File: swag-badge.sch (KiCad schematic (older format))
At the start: 22 parts, among them J1 OLED_1, J10 Edge_pad, J11 Edge_pad, J12 Breakout_LHS, J13 Breakout_RHS, J2 OLED_2, J3 SAO_1, J4 SAO_2, J5 SAO_3, J6 SAO_4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

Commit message: Minor footprint work
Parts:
- added H3: MountingHole, SwagBadge:Lanyard_Hole_3mm, symbol Mechanical:MountingHole
- J12: renamed from J13; value Breakout_RHS -> Breakout_LHS; footprint Pin_Headers:Pin_Header_Angled_1x08_Pitch2.54mm -> SwagBadge:Pin_Header_Angled_1x08_Pitch2.54mm
- J13: renamed from J12; value Breakout_LHS -> Breakout_RHS; footprint Pin_Headers:Pin_Header_Angled_1x08_Pitch2.54mm -> SwagBadge:Pin_Header_Angled_1x08_Pitch2.54mm
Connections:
- net +3V3: now also J12.8 (Pin_8), J13.8 (Pin_8); no longer J12.1 (Pin_1), J13.1 (Pin_1)
- net GND: now also J12.1 (Pin_1), J13.1 (Pin_1); no longer J12.8 (Pin_8), J13.8 (Pin_8)
- net GPIO0: now also J12.4 (Pin_4); no longer J12.5 (Pin_5)
- net GPIO13: now also J12.2 (Pin_2); no longer J12.7 (Pin_7)
- net GPIO18: now also J12.7 (Pin_7); no longer J12.2 (Pin_2)
- net GPIO2: now also J12.3 (Pin_3); no longer J12.6 (Pin_6)
- net GPIO25: now also J13.3 (Pin_3); no longer J13.6 (Pin_6)
- net GPIO26: now also J13.2 (Pin_2); no longer J13.7 (Pin_7)
- net GPIO32: now also J13.5 (Pin_5); no longer J13.4 (Pin_4)
- net GPIO33: now also J13.4 (Pin_4); no longer J13.5 (Pin_5)
- net GPIO34: now also J13.7 (Pin_7); no longer J13.2 (Pin_2)
- net GPIO35: now also J13.6 (Pin_6); no longer J13.3 (Pin_3)
- net GPIO4: now also J12.5 (Pin_5); no longer J12.4 (Pin_4)
- net GPIO5: now also J12.6 (Pin_6); no longer J12.3 (Pin_3)
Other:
- moved on the sheet: J13
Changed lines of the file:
@@
-$EndComp
-$Comp
-L Connector_Generic:Conn_01x08 J13
-U 1 1 5F7E62CC
-P 7800 2000
-F 0 "J13" H 7750 2500 50  0000 L CNN
-F 1 "Breakout_RHS" H 7700 2400 50  0000 L CNN
-F 2 "Pin_Headers:Pin_Header_Angled_1x08_Pitch2.54mm" H 7800 2000 50  0001 C CNN
-F 3 "~" H 7800 2000 50  0001 C CNN
-	1    7800 2000
-	-1   0    0    -1
 $EndComp
 $Comp
@@
 $EndComp
 $Comp
-L power:+3V3 #PWR?
+L power:+3V3 #PWR0115
 U 1 1 5F810C4A
 P 8150 1600
-F 0 "#PWR?" H 8150 1450 50  0001 C CNN
+F 0 "#PWR0115" H 8150 1450 50  0001 C CNN
 F 1 "+3V3" H 8165 1773 50  0000 C CNN
 F 2 "" H 8150 1600 50  0001 C CNN
@@
 $EndComp
 $Comp
-L power:GND #PWR?
+L power:GND #PWR0116
 U 1 1 5F816772
-P 6350 2500
-F 0 "#PWR?" H 6350 2250 50  0001 C CNN
-F 1 "GND" H 6355 2327 50  0000 C CNN
-F 2 "" H 6350 2500 50  0001 C CNN
-F 3 "" H 6350 2500 50  0001 C CNN
-	1    6350 2500
+P 8850 2500
+F 0 "#PWR0116" H 8850 2250 50  0001 C CNN
+F 1 "GND" H 8855 2327 50  0000 C CNN
+F 2 "" H 8850 2500 50  0001 C CNN
+F 3 "" H 8850 2500 50  0001 C CNN
+	1    8850 2500
 	1    0    0    -1
 $EndComp
 $Comp
-L power:GND #PWR?
+L power:GND #PWR0117
 U 1 1 5F816BF9
 P 8100 2500
-F 0 "#PWR?" H 8100 2250 50  0001 C CNN
+F 0 "#PWR0117" H 8100 2250 50  0001 C CNN
 F 1 "GND" H 8105 2327 50  0000 C CNN
 F 2 "" H 8100 2500 50  0001 C CNN
@@
 $EndComp
 Wire Wire Line
-	6450 2400 6350 2400
+	8950 2400 8850 2400
 Wire Wire Line
-	6350 2400 6350 2500
+	8850 2400 8850 2500
 Wire Wire Line
 	8000 2400 8100 2400
@@
 	8150 1700 8150 1600
 Wire Wire Line
-	6450 1700 6350 1700
+	8950 1700 8850 1700
 Wire Wire Line
-	6350 1700 6350 1600
+	8850 1700 8850 1600
 Text Label 8400 2200 2    70   ~ 0
 GPIO2
@@
 Wire Wire Line
 	8000 2300 8400 2300
-Text Label 6050 1800 0    70   ~ 0
+Text Label 8550 1800 0    70   ~ 0
 GPIO34
-Text Label 6050 1900 0    70   ~ 0
+Text Label 8550 1900 0    70   ~ 0
 GPIO35
-Text Label 6050 2000 0    70   Italic 0
+Text Label 8550 2000 0    70   Italic 0
 GPIO32
-Text Label 6050 2100 0    70   Italic 0
+Text Label 8550 2100 0    70   Italic 0
 GPIO33
-Text Label 6050 2200 0    70   Italic 0
+Text Label 8550 2200 0    70   Italic 0
 GPIO25
-Text Label 6050 2300 0    70   Italic 0
+Text Label 8550 2300 0    70   Italic 0
 GPIO26
 Wire Wire Line
-	6450 2300 6050 2300
+	8950 2300 8550 2300
 Wire Wire Line
-	6050 2200 6450 2200
+	8550 2200 8950 2200
 Wire Wire Line
-	6050 2100 6450 2100
+	8550 2100 8950 2100
 Wire Wire Line
-	6050 2000 6450 2000
+	8550 2000 8950 2000
 Wire Wire Line
-	6050 1900 6450 1900
+	8550 1900 8950 1900
 Wire Wire Line
-	6050 1800 6450 1800
+	8550 1800 8950 1800
 $Comp
 L Mechanical:MountingHole H4
@@
 $EndComp
 $Comp
-L Connector_Generic:Conn_01x08 J12
-U 1 1 5F7FE834
-P 6650 2000
-F 0 "J12" H 6600 2550 50  0000 L CNN
-F 1 "Breakout_LHS" H 6400 2450 50  0000 L CNN
-F 2 "Pin_Headers:Pin_Header_Angled_1x08_Pitch2.54mm" H 6650 2000 50  0001 C CNN
-F 3 "~" H 6650 2000 50  0001 C CNN
-	1    6650 2000
-	1    0    0    -1
-$EndComp
-$Comp
-L power:+3V3 #PWR?
+L power:+3V3 #PWR0118
 U 1 1 5F85A5CE
-P 6350 1600
-F 0 "#PWR?" H 6350 1450 50  0001 C CNN
-F 1 "+3V3" H 6365 1773 50  0000 C CNN
-F 2 "" H 6350 1600 50  0001 C CNN
-F 3 "" H 6350 1600 50  0001 C CNN
-	1    6350 1600
+P 8850 1600
+F 0 "#PWR0118" H 8850 1450 50  0001 C CNN
+F 1 "+3V3" H 8865 1773 50  0000 C CNN
+F 2 "" H 8850 1600 50  0001 C CNN
+F 3 "" H 8850 1600 50  0001 C CNN
+	1    8850 1600
 	1    0    0    -1
 $EndComp
 Text Label 8400 2300 2    70   ~ 0
 GPIO13
+$Comp
+L Connector_Generic:Conn_01x08 J13
+U 1 1 5F7FE834
+P 9150 2100
+F 0 "J13" H 9050 1450 50  0000 L CNN
+F 1 "Breakout_RHS" H 8900 1550 50  0000 L CNN
+F 2 "SwagBadge:Pin_Header_Angled_1x08_Pitch2.54mm" H 9150 2100 50  0001 C CNN
+F 3 "~" H 9150 2100 50  0001 C CNN
+	1    9150 2100
+	1    0    0    1
+$EndComp
+$Comp
+L Connector_Generic:Conn_01x08 J12
+U 1 1 5F7E62CC
+P 7800 2100
+F 0 "J12" H 7750 1450 50  0000 L CNN
+F 1 "Breakout_LHS" H 7600 1550 50  0000 L CNN
+F 2 "SwagBadge:Pin_Header_Angled_1x08_Pitch2.54mm" H 7800 2100 50  0001 C CNN
+F 3 "~" H 7800 2100 50  0001 C CNN
+	1    7800 2100
+	-1   0    0    1
+$EndComp
+$Comp
+L Mechanical:MountingHole H3
+U 1 1 5F800940
+P 5800 6400
+F 0 "H3" H 5900 6446 50  0000 L CNN
+F 1 "MountingHole" H 5900 6355 50  0000 L CNN
+F 2 "SwagBadge:Lanyard_Hole_3mm" H 5800 6400 50  0001 C CNN
+F 3 "~" H 5800 6400 50  0001 C CNN
+	1    5800 6400
+	1    0    0    -1
+$EndComp
 $EndSCHEMATC

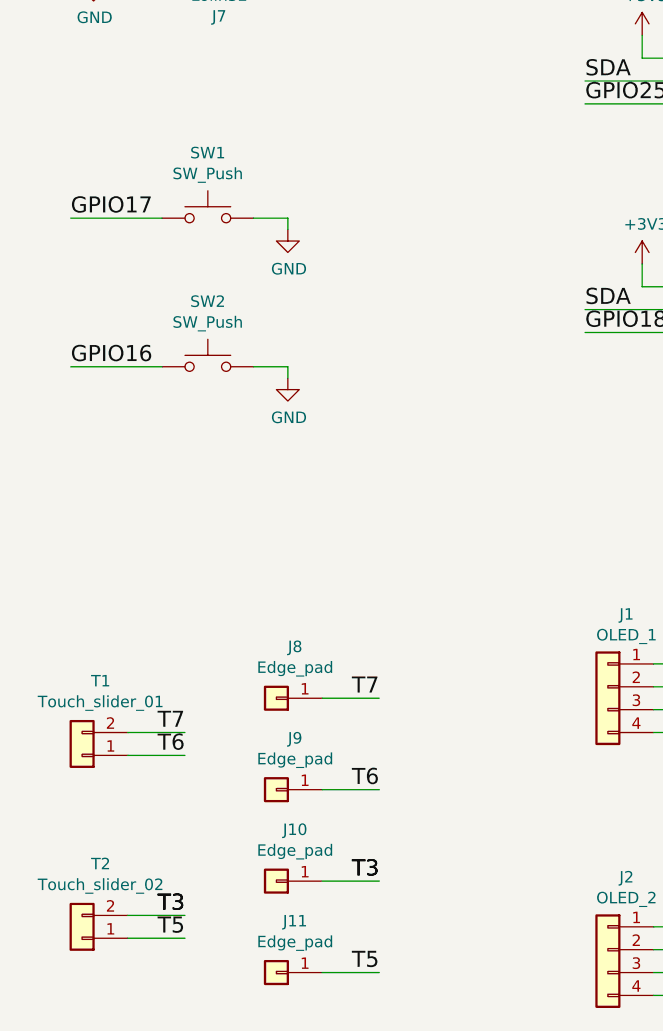
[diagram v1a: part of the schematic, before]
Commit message: Updated Component names to reflect purpose.
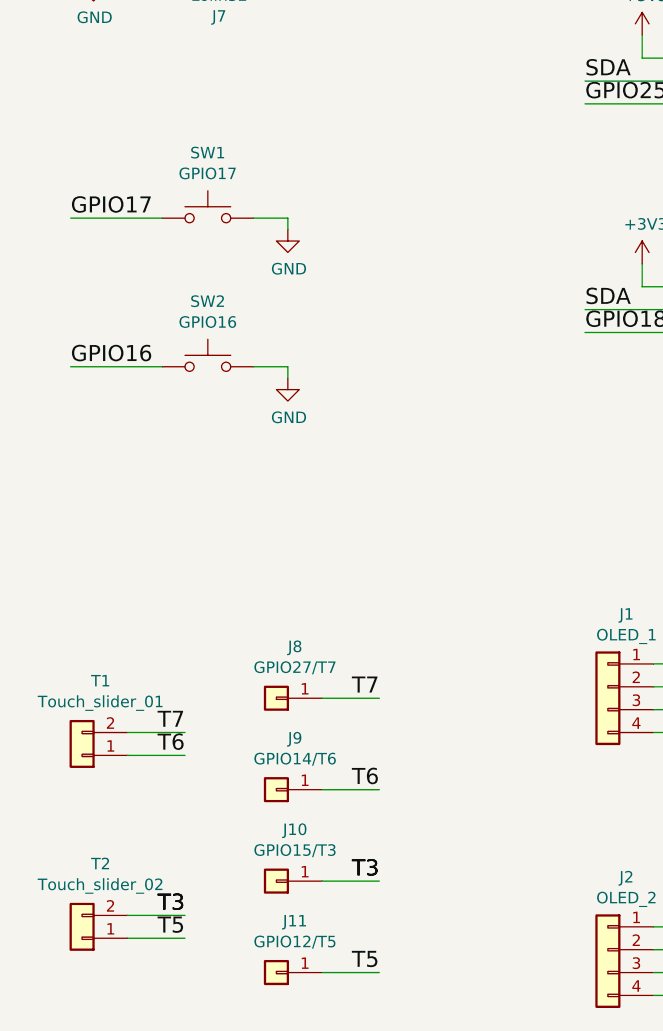
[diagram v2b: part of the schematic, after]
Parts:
- J10: value Edge_pad -> GPIO15/T3
- J11: value Edge_pad -> GPIO12/T5
- J8: value Edge_pad -> GPIO27/T7
- J9: value Edge_pad -> GPIO14/T6
- SW1: value SW_Push -> GPIO17
- SW2: value SW_Push -> GPIO16
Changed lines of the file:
@@
 P 1800 3700
 F 0 "SW1" H 1800 3985 50  0000 C CNN
-F 1 "SW_Push" H 1800 3894 50  0000 C CNN
+F 1 "GPIO17" H 1800 3894 50  0000 C CNN
 F 2 "SwagBadge:SW_SPST_6x3mm" H 1800 3900 50  0001 C CNN
 F 3 "~" H 1800 3900 50  0001 C CNN
@@
 P 1800 4350
 F 0 "SW2" H 1800 4635 50  0000 C CNN
-F 1 "SW_Push" H 1800 4544 50  0000 C CNN
+F 1 "GPIO16" H 1800 4544 50  0000 C CNN
 F 2 "SwagBadge:SW_SPST_6x3mm" H 1800 4550 50  0001 C CNN
 F 3 "~" H 1800 4550 50  0001 C CNN
@@
 P 2100 5800
 F 0 "J8" H 2018 5575 50  0000 C CNN
-F 1 "Edge_pad" H 2018 5666 50  0000 C CNN
+F 1 "GPIO27/T7" H 2018 5666 50  0000 C CNN
 F 2 "SwagBadge:Strain_Pad" H 2100 5800 50  0001 C CNN
 F 3 "~" H 2100 5800 50  0001 C CNN
@@
 P 2100 6200
 F 0 "J9" H 2018 5975 50  0000 C CNN
-F 1 "Edge_pad" H 2018 6066 50  0000 C CNN
+F 1 "GPIO14/T6" H 2018 6066 50  0000 C CNN
 F 2 "SwagBadge:Strain_Pad" H 2100 6200 50  0001 C CNN
 F 3 "~" H 2100 6200 50  0001 C CNN
@@
 P 2100 6600
 F 0 "J10" H 2018 6375 50  0000 C CNN
-F 1 "Edge_pad" H 2018 6466 50  0000 C CNN
+F 1 "GPIO15/T3" H 2018 6466 50  0000 C CNN
 F 2 "SwagBadge:Strain_Pad" H 2100 6600 50  0001 C CNN
 F 3 "~" H 2100 6600 50  0001 C CNN
@@
 P 2100 7000
 F 0 "J11" H 2018 6775 50  0000 C CNN
-F 1 "Edge_pad" H 2018 6866 50  0000 C CNN
+F 1 "GPIO12/T5" H 2018 6866 50  0000 C CNN
 F 2 "SwagBadge:Strain_Pad" H 2100 7000 50  0001 C CNN
 F 3 "~" H 2100 7000 50  0001 C CNN

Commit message: Welcome to the grid
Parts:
- J3: value SAO_1 -> SAO_2
- J4: value SAO_2 -> SAO_1
- J5: value SAO_3 -> SAO_4
- J6: value SAO_4 -> SAO_3
- L1: footprint SwagBadge:Logo_LCA2021_04 -> SwagBadge:Logo_LCA2021_04A
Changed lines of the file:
@@
 P 4000 1150
 F 0 "J3" H 4050 1467 50  0000 C CNN
-F 1 "SAO_1" H 4050 1376 50  0000 C CNN
+F 1 "SAO_2" H 4050 1376 50  0000 C CNN
 F 2 "SwagBadge:SAO_Header_6-Pin" H 4000 1150 50  0001 C CNN
 F 3 "~" H 4000 1150 50  0001 C CNN
@@
 P 4000 2100
 F 0 "J4" H 4050 2417 50  0000 C CNN
-F 1 "SAO_2" H 4050 2326 50  0000 C CNN
+F 1 "SAO_1" H 4050 2326 50  0000 C CNN
 F 2 "SwagBadge:SAO_Header_6-Pin" H 4000 2100 50  0001 C CNN
 F 3 "~" H 4000 2100 50  0001 C CNN
@@
 P 4000 3100
 F 0 "J5" H 4050 3417 50  0000 C CNN
-F 1 "SAO_3" H 4050 3326 50  0000 C CNN
+F 1 "SAO_4" H 4050 3326 50  0000 C CNN
 F 2 "SwagBadge:SAO_Header_6-Pin" H 4000 3100 50  0001 C CNN
 F 3 "~" H 4000 3100 50  0001 C CNN
@@
 P 4000 4100
 F 0 "J6" H 4050 4417 50  0000 C CNN
-F 1 "SAO_4" H 4050 4326 50  0000 C CNN
+F 1 "SAO_3" H 4050 4326 50  0000 C CNN
 F 2 "SwagBadge:SAO_Header_6-Pin" H 4000 4100 50  0001 C CNN
 F 3 "~" H 4000 4100 50  0001 C CNN
@@
 F 0 "L1" H 6300 5403 50  0000 C CNN
 F 1 "Logo_LCA2021" H 6300 5312 50  0000 C CNN
-F 2 "SwagBadge:Logo_LCA2021_04" H 6300 4900 50  0001 C CNN
+F 2 "SwagBadge:Logo_LCA2021_04A" H 6300 4900 50  0001 C CNN
 F 3 "" H 6300 4900 50  0001 C CNN
 	1    6300 5100

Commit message: Routing started
Feel free to delete and start again. Just noodling.
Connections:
- net GPIO25: now also J5.4 (Pin_4); no longer J5.3 (Pin_3)
- net GPIO26: now also J5.3 (Pin_3); no longer J5.4 (Pin_4)
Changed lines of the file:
@@
 SDA
 Text Label 4750 3200 2    70   ~ 0
+GPIO25
+Text Label 3450 3200 0    70   ~ 0
 GPIO26
-Text Label 3450 3200 0    70   ~ 0
-GPIO25
 $Comp
 L Connector_Generic:Conn_01x01 J8

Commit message: Starting to Route
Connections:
- net GPIO12: now also T1.1 (Pin_1); no longer T2.1 (Pin_1)
- net GPIO14: now also T2.1 (Pin_1); no longer T1.1 (Pin_1)
- net GPIO15: now also T1.2 (Pin_2); no longer T2.2 (Pin_2)
- net GPIO27: now also T2.2 (Pin_2); no longer T1.2 (Pin_2)
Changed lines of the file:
@@
 Text Label 1200 4350 0    70   ~ 0
 GPIO16
-Text Label 1700 5950 2    70   ~ 0
+Text Label 1700 6750 2    70   ~ 0
 T7
+Text Label 1700 6850 2    70   ~ 0
+T6
 Text Label 1700 6050 2    70   ~ 0
-T6
-Text Label 1700 6850 2    70   ~ 0
 T5
 Wire Wire Line
@@
 	-1   0    0    1
 $EndComp
-Text Label 1700 6750 2    70   ~ 0
-T3
-Text Label 1700 6750 2    70   ~ 0
+Text Label 1700 5950 2    70   ~ 0
 T3
 Wire Wire Line

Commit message: More routing.
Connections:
- net GPIO19: now also J4.4 (Pin_4); no longer J4.3 (Pin_3)
- net GPIO22: now also J4.3 (Pin_3); no longer J4.4 (Pin_4)
- net GPIO25: now also J13.6 (Pin_6); no longer J13.3 (Pin_3)
- net GPIO26: now also J13.7 (Pin_7); no longer J13.2 (Pin_2)
- net GPIO32: now also J13.4 (Pin_4); no longer J13.5 (Pin_5)
- net GPIO33: now also J13.5 (Pin_5); no longer J13.4 (Pin_4)
- net GPIO34: now also J13.2 (Pin_2); no longer J13.7 (Pin_7)
- net GPIO35: now also J13.3 (Pin_3); no longer J13.6 (Pin_6)
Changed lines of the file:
@@
 	1    0    0    -1
 $EndComp
+Text Label 3450 2200 0    70   ~ 0
+GPIO22
 Text Label 4750 2200 2    70   ~ 0
-GPIO22
-Text Label 3450 2200 0    70   ~ 0
 GPIO19
 Text Label 3450 1150 0    70   ~ 0
@@
 Wire Wire Line
 	1200 4350 1600 4350
-Text Label 1200 3700 0    70   ~ 0
-GPIO17
-Text Label 1200 4350 0    70   ~ 0
-GPIO16
 Text Label 1700 6750 2    70   ~ 0
 T7
@@
 Wire Wire Line
 	8000 2300 8400 2300
-Text Label 8550 1800 0    70   ~ 0
+Text Label 8550 2300 0    70   ~ 0
 GPIO34
-Text Label 8550 1900 0    70   ~ 0
+Text Label 8550 2200 0    70   ~ 0
 GPIO35
+Text Label 8550 2100 0    70   Italic 0
+GPIO32
 Text Label 8550 2000 0    70   Italic 0
-GPIO32
-Text Label 8550 2100 0    70   Italic 0
 GPIO33
-Text Label 8550 2200 0    70   Italic 0
+Text Label 8550 1900 0    70   Italic 0
 GPIO25
-Text Label 8550 2300 0    70   Italic 0
+Text Label 8550 1800 0    70   Italic 0
 GPIO26
 Wire Wire Line
@@
 	1    0    0    -1
 $EndComp
+Text Label 1200 4350 0    70   ~ 0
+GPIO16
+Text Label 1200 3700 0    70   ~ 0
+GPIO17
 $EndSCHEMATC

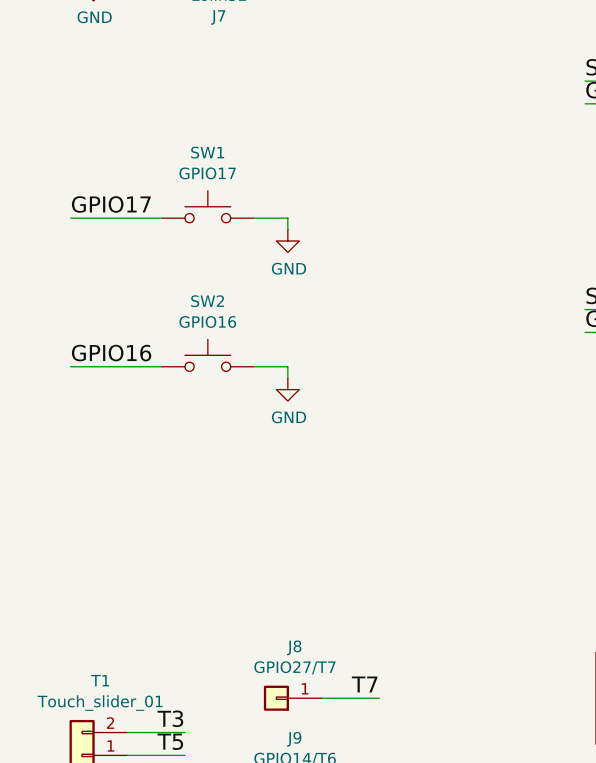
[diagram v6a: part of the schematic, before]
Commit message: Adding extra switches for dual footprint.
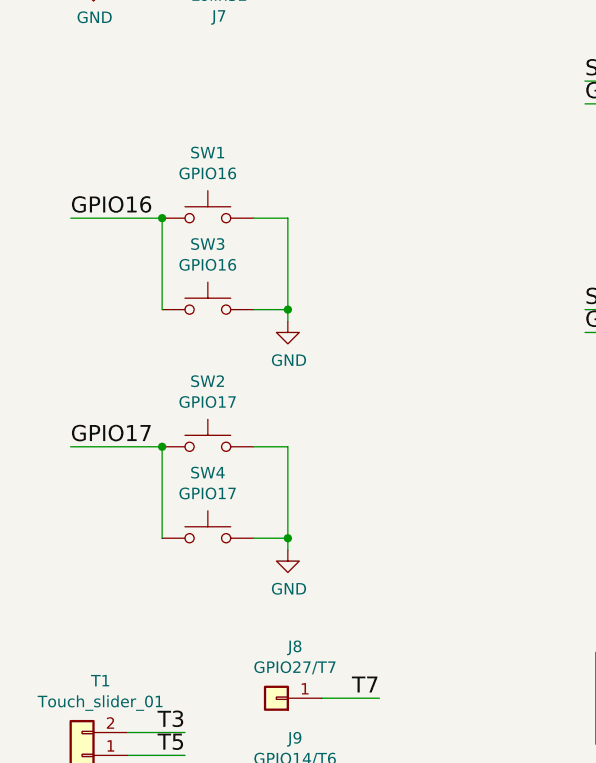
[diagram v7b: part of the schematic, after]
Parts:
- added SW3: GPIO16, SwagBadge:SW_SPST_3x4mm, symbol Switch:SW_Push
- added SW4: GPIO17, SwagBadge:SW_SPST_3x4mm, symbol Switch:SW_Push
- SW1: value GPIO17 -> GPIO16
- SW2: value GPIO16 -> GPIO17
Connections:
- net GND: now also SW3.2, SW4.2
- net GPIO16: now also SW1.1, SW3.1; no longer SW2.1
- net GPIO17: now also SW2.1, SW4.1; no longer SW1.1
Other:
- moved on the sheet: SW2
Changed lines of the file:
@@
 P 1800 3700
 F 0 "SW1" H 1800 3985 50  0000 C CNN
-F 1 "GPIO17" H 1800 3894 50  0000 C CNN
+F 1 "GPIO16" H 1800 3894 50  0000 C CNN
 F 2 "SwagBadge:SW_SPST_6x3mm" H 1800 3900 50  0001 C CNN
 F 3 "~" H 1800 3900 50  0001 C CNN
@@
 L Switch:SW_Push SW2
 U 1 1 5F7BF1A3
-P 1800 4350
-F 0 "SW2" H 1800 4635 50  0000 C CNN
-F 1 "GPIO16" H 1800 4544 50  0000 C CNN
-F 2 "SwagBadge:SW_SPST_6x3mm" H 1800 4550 50  0001 C CNN
-F 3 "~" H 1800 4550 50  0001 C CNN
-	1    1800 4350
+P 1800 4700
+F 0 "SW2" H 1800 4985 50  0000 C CNN
+F 1 "GPIO17" H 1800 4894 50  0000 C CNN
+F 2 "SwagBadge:SW_SPST_6x3mm" H 1800 4900 50  0001 C CNN
+F 3 "~" H 1800 4900 50  0001 C CNN
+	1    1800 4700
 	1    0    0    -1
 $EndComp
@@
 L power:GND #PWR0104
 U 1 1 5F7C3E3D
-P 2150 3750
-F 0 "#PWR0104" H 2150 3500 50  0001 C CNN
-F 1 "GND" H 2155 3577 50  0000 C CNN
-F 2 "" H 2150 3750 50  0001 C CNN
-F 3 "" H 2150 3750 50  0001 C CNN
-	1    2150 3750
+P 2150 4150
+F 0 "#PWR0104" H 2150 3900 50  0001 C CNN
+F 1 "GND" H 2155 3977 50  0000 C CNN
+F 2 "" H 2150 4150 50  0001 C CNN
+F 3 "" H 2150 4150 50  0001 C CNN
+	1    2150 4150
 	1    0    0    -1
 $EndComp
@@
 	2000 3700 2150 3700
 Wire Wire Line
-	2150 3700 2150 3750
+	2150 3700 2150 4100
 Wire Wire Line
 	1200 3700 1600 3700
@@
 L power:GND #PWR0114
 U 1 1 5F7CDE40
-P 2150 4400
-F 0 "#PWR0114" H 2150 4150 50  0001 C CNN
-F 1 "GND" H 2155 4227 50  0000 C CNN
-F 2 "" H 2150 4400 50  0001 C CNN
-F 3 "" H 2150 4400 50  0001 C CNN
-	1    2150 4400
-	1    0    0    -1
-$EndComp
-Wire Wire Line
-	2000 4350 2150 4350
-Wire Wire Line
-	2150 4350 2150 4400
-Wire Wire Line
-	1200 4350 1600 4350
+P 2150 5150
+F 0 "#PWR0114" H 2150 4900 50  0001 C CNN
+F 1 "GND" H 2155 4977 50  0000 C CNN
+F 2 "" H 2150 5150 50  0001 C CNN
+F 3 "" H 2150 5150 50  0001 C CNN
+	1    2150 5150
+	1    0    0    -1
+$EndComp
+Wire Wire Line
+	2000 4700 2150 4700
+Wire Wire Line
+	1200 4700 1600 4700
 Text Label 1700 6750 2    70   ~ 0
 T7
@@
 	1    0    0    -1
 $EndComp
-Text Label 1200 4350 0    70   ~ 0
+Text Label 1200 3700 0    70   ~ 0
 GPIO16
-Text Label 1200 3700 0    70   ~ 0
+Text Label 1200 4700 0    70   ~ 0
 GPIO17
+$Comp
+L Switch:SW_Push SW3
+U 1 1 5F83CA35
+P 1800 4100
+F 0 "SW3" H 1800 4385 50  0000 C CNN
+F 1 "GPIO16" H 1800 4294 50  0000 C CNN
+F 2 "SwagBadge:SW_SPST_3x4mm" H 1800 4300 50  0001 C CNN
+F 3 "~" H 1800 4300 50  0001 C CNN
+	1    1800 4100
+	1    0    0    -1
+$EndComp
+Wire Wire Line
+	1600 3700 1600 4100
+Connection ~ 1600 3700
+Wire Wire Line
+	2000 4100 2150 4100
+Connection ~ 2150 4100
+Wire Wire Line
+	2150 4100 2150 4150
+$Comp
+L Switch:SW_Push SW4
+U 1 1 5F84DC35
+P 1800 5100
+F 0 "SW4" H 1800 5385 50  0000 C CNN
+F 1 "GPIO17" H 1800 5294 50  0000 C CNN
+F 2 "SwagBadge:SW_SPST_3x4mm" H 1800 5300 50  0001 C CNN
+F 3 "~" H 1800 5300 50  0001 C CNN
+	1    1800 5100
+	1    0    0    -1
+$EndComp
+Wire Wire Line
+	1600 5100 1600 4700
+Connection ~ 1600 4700
+Wire Wire Line
+	2150 4700 2150 5100
+Wire Wire Line
+	2000 5100 2150 5100
+Connection ~ 2150 5100
+Wire Wire Line
+	2150 5100 2150 5150
 $EndSCHEMATC

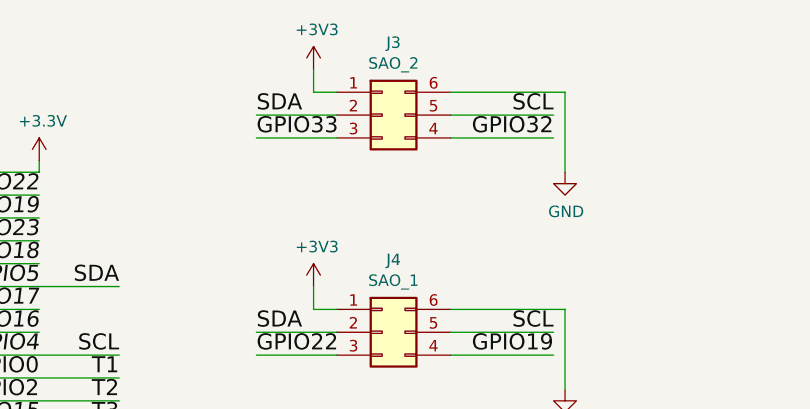
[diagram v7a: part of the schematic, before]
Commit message: Routing first pass complete.
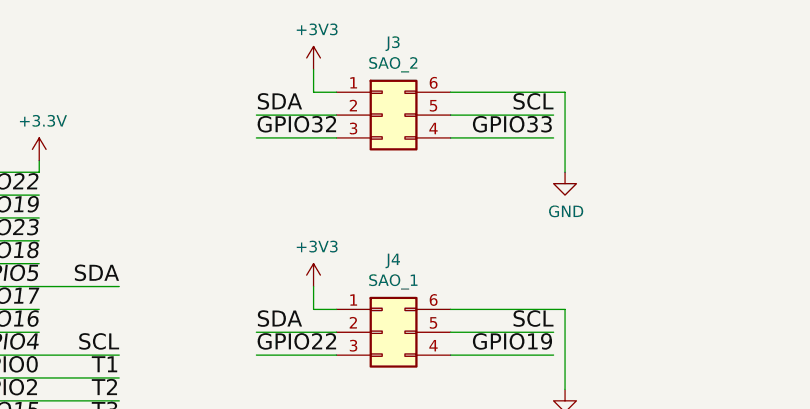
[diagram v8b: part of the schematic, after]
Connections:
- net GPIO32: now also J3.3 (Pin_3); no longer J3.4 (Pin_4)
- net GPIO33: now also J3.4 (Pin_4); no longer J3.3 (Pin_3)
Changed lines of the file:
@@
 Text Label 4750 1150 2    70   ~ 0
 SCL
-Text Label 4750 1250 2    70   ~ 0
+Text Label 3450 1250 0    70   ~ 0
 GPIO32
 Text Label 4750 2100 2    70   ~ 0
@@
 Text Label 3450 3100 0    70   ~ 0
 SDA
-Text Label 3450 1250 0    70   ~ 0
+Text Label 4750 1250 2    70   ~ 0
 GPIO33
 Text Label 4750 4200 2    70   ~ 0
